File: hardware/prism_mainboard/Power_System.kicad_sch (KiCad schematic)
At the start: 0 parts

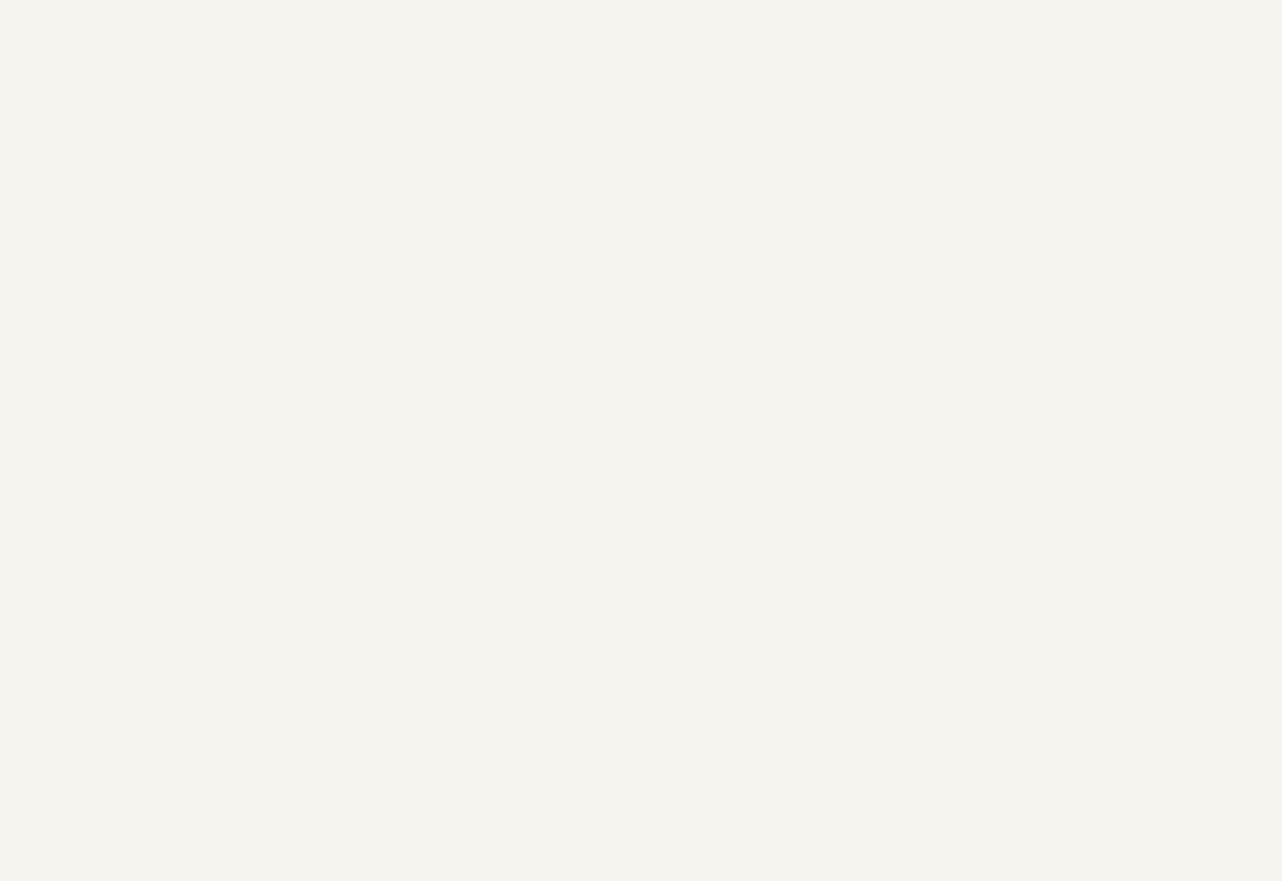
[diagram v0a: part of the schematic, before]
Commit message: KiCAD Update
Added Power System Schematics. Decided on a 4 in 1 Buck and LDO, LP87222TQ1, for 3.3V and 1.8V LDO, and 1.8V and 1.0V Buck converter.
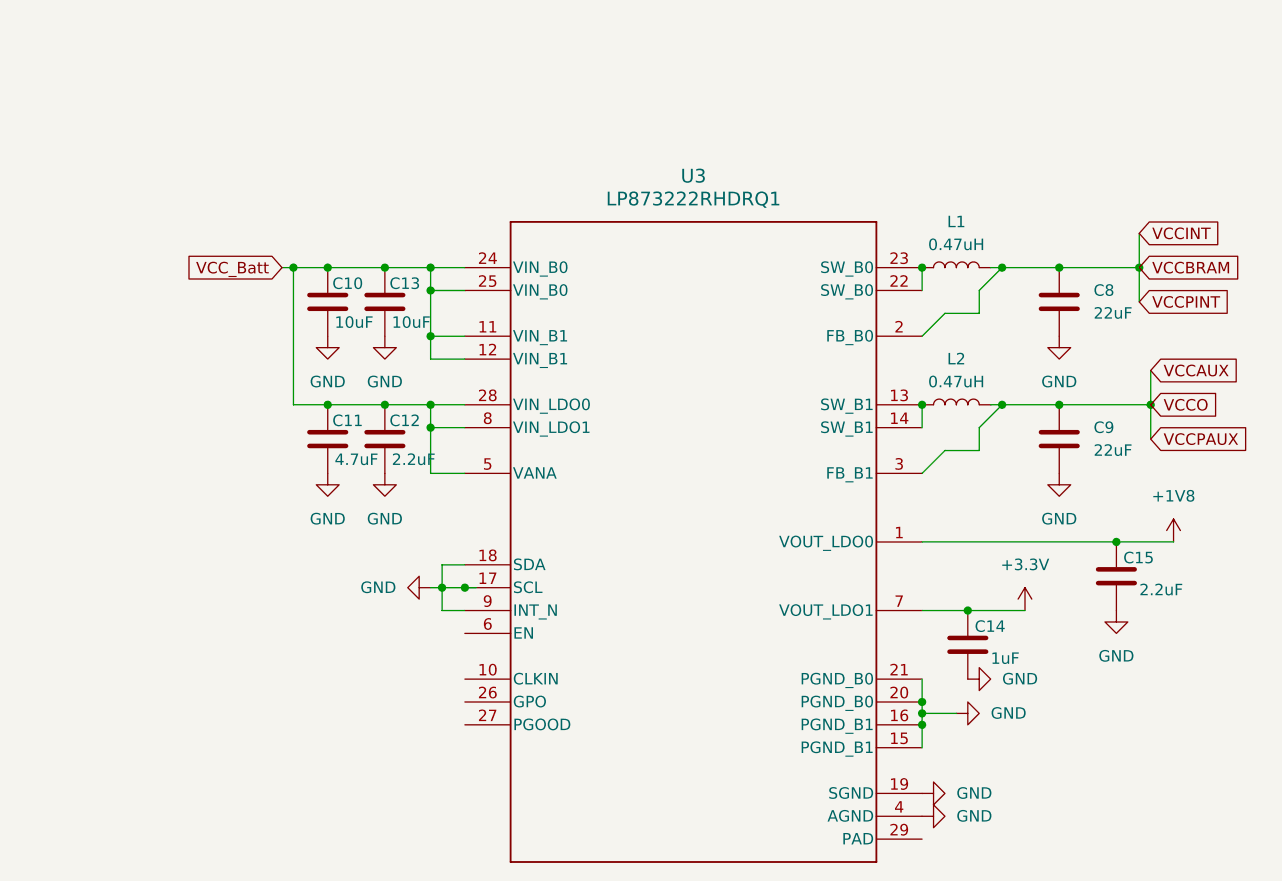
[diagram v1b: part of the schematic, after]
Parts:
- added C10, C13: 10uF, Capacitor_SMD:C_0805_2012Metric, symbol Device:C
- added C11: 4.7uF, Capacitor_SMD:C_0805_2012Metric, symbol Device:C
- added C12, C15: 2.2uF, Capacitor_SMD:C_0201_0603Metric, symbol Device:C
- added C14: 1uF, Capacitor_SMD:C_0201_0603Metric, symbol Device:C
- added C8, C9: 22uF, Capacitor_SMD:C_1206_3216Metric, symbol Device:C
- added L1, L2: 0.47uH, Inductor_SMD:L_0805_2012Metric, symbol Device:L
- added U3: LP873222RHDRQ1, RHD0028W, symbol 2026-05-18_00-35-41:LP873222RHDRQ1
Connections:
- net VCCAUX: now also C9.1, L2.2
- net VCCBRAM: now also C8.1, L1.2
- net VCC_Batt: now also C10.1, C11.1, C12.1, C13.1, U3.11 (VIN_B1), U3.12 (VIN_B1), U3.24 (VIN_B0), U3.25 (VIN_B0), U3.28 (VIN_LDO0), U3.5 (VANA), U3.8 (VIN_LDO1)
- new net: L2.1, U3.13 (SW_B1), U3.14 (SW_B1)
- new net: L1.1, U3.22 (SW_B0), U3.23 (SW_B0)
- new net +1V8: C15.1, U3.1 (VOUT_LDO0)
- new net +3.3V: C14.1, U3.7 (VOUT_LDO1)
- new net GND: C10.2, C11.2, C12.2, C13.2, C14.2, C15.2, C8.2, C9.2, U3.15 (PGND_B1), U3.16 (PGND_B1), U3.17 (SCL), U3.18 (SDA), U3.19 (SGND), U3.20 (PGND_B0), U3.21 (PGND_B0), U3.4 (AGND), U3.9 (INT_N)

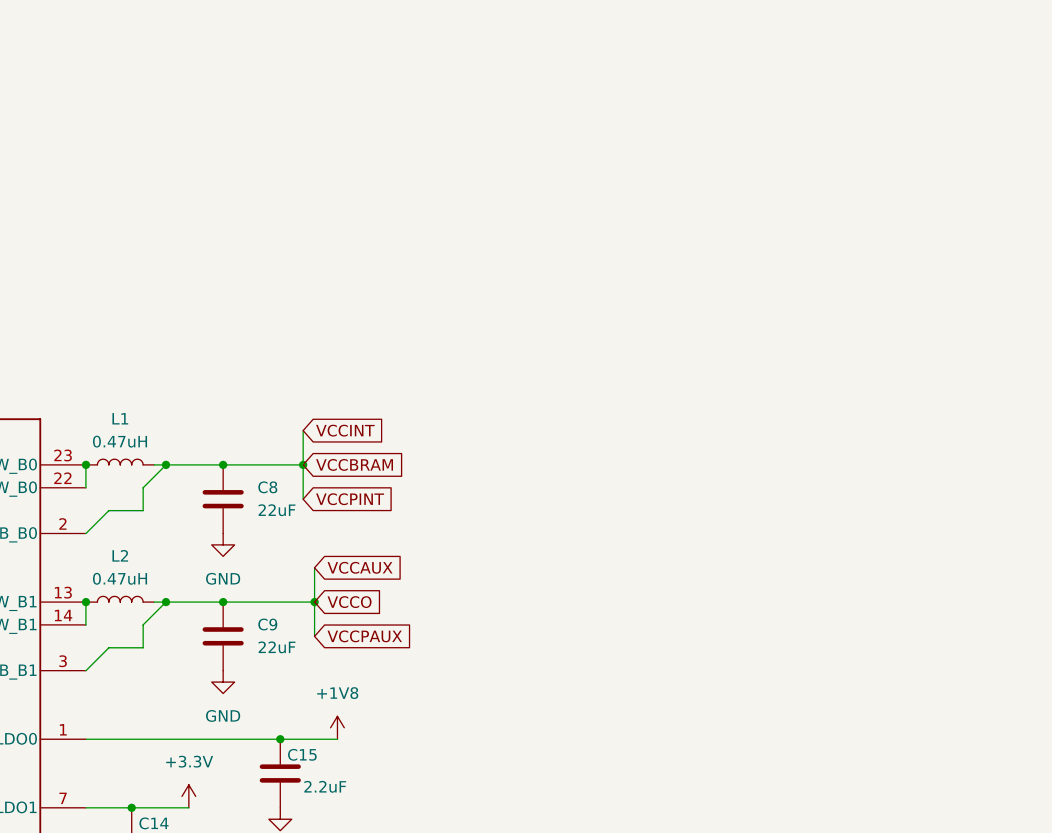
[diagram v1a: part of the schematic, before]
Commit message: Schematics
More schematics updates, moving to Desktop for editing. Continued with power usage, debating use of Dedicated DDR3/3L power IC instead of using LDO and Buck from mainboard power.
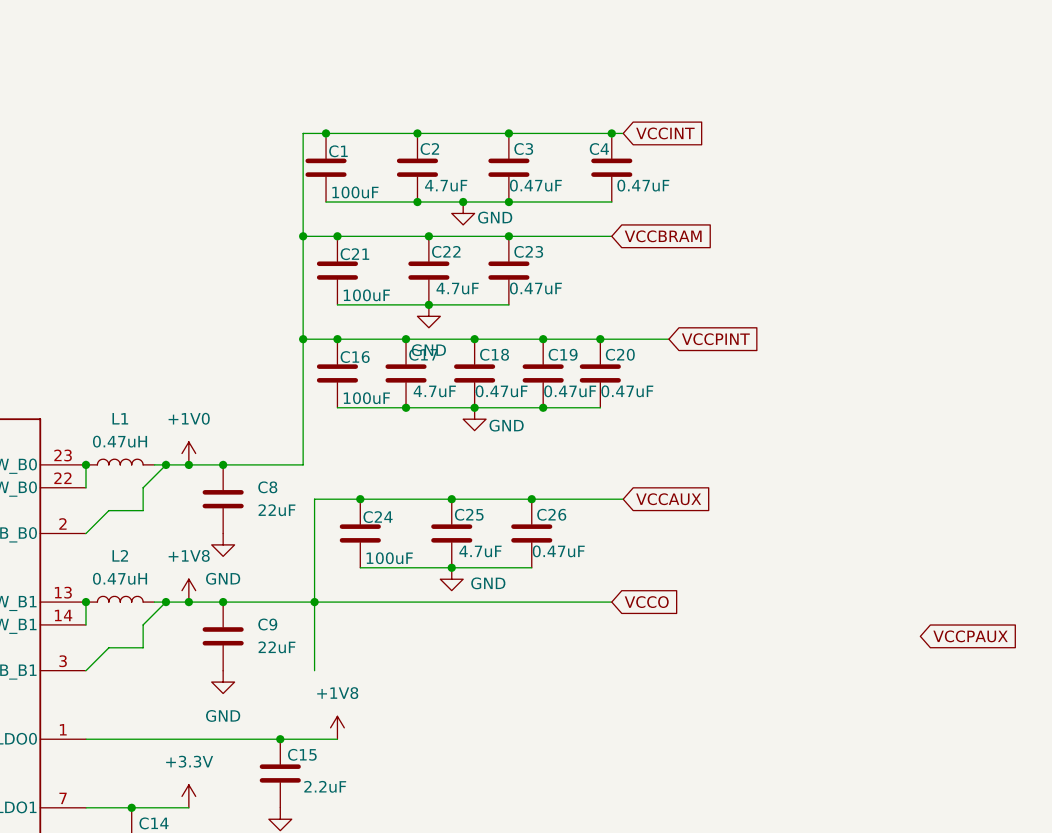
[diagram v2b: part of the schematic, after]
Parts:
- added C1, C16, C21, C24: 100uF, symbol Device:C
- added C17, C2, C22, C25: 4.7uF, symbol Device:C
- added C18, C19, C20, C23, C26, C3, C4: 0.47uF, symbol Device:C
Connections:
- net VCCAUX is gone; now on net +1V8: C9.1, L2.2
- net +1V8: now also C24.1, C25.1, C26.1
- net GND: now also C1.2, C16.2, C17.2, C18.2, C19.2, C2.2, C20.2, C21.2, C22.2, C23.2, C24.2, C25.2, C26.2, C3.2, C4.2
- net VCCBRAM renamed +1V0
- net +1V0: now also C1.1, C16.1, C17.1, C18.1, C19.1, C2.1, C20.1, C21.1, C22.1, C23.1, C3.1, C4.1

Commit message: Removed Protoflow
Removed protoflow because it has not advanced enough to help in any substantial way, going back to KiCAD
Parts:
- added C27, C28: 22uF, ProtoFlow.pretty:C0805, symbol Device:C
- added U4: 100uF, symbol Device:C
- added U5: 0.47uF, symbol Device:C
- added U6: 4.7uF, symbol Device:C
- added U7: GND, symbol power:GND
- C1, C10, C11, C12, C13, C14, C15, C16, C17, C18, C19, C2, C20, C21, C22, C23, C24, C25, C26, C3, C4, C8, C9, L1, L2, U3: Protoflow_Source (none) -> kicad
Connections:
- net VCCBRAM: now reaches U3.2 (FB_B0)
- net VCCBRAM: now also C1.1, C16.1, C17.1, C18.1, C19.1, C20.1, C21.1, C22.1, C23.1, C4.1, C8.1, L1.2
- net VCCAUX: now reaches U3.3 (FB_B1)
- net VCCAUX: now also C24.1, C25.1, C26.1, C9.1, L2.2
- removed net +1V0: C1.1, C16.1, C17.1, C18.1, C19.1, C2.1, C20.1, C21.1, C22.1, C23.1, C3.1, C4.1, C8.1, L1.2
- removed net +1V8: C15.1, C24.1, C25.1, C26.1, C9.1, L2.2, U3.1 (VOUT_LDO0)
- net +3.3V: no longer names the net of C14.1, U3.7 (VOUT_LDO1)
- removed net GND: C1.2, C10.2, C11.2, C12.2, C13.2, C14.2, C15.2, C16.2, C17.2, C18.2, C19.2, C2.2, C20.2, C21.2, C22.2, C23.2, C24.2, C25.2, C26.2, C3.2, C4.2, C8.2, C9.2, U3.15 (PGND_B1), U3.16 (PGND_B1), U3.17 (SCL), U3.18 (SDA), U3.19 (SGND), U3.20 (PGND_B0), U3.21 (PGND_B0), U3.4 (AGND), U3.9 (INT_N)
- new net: C16.2, C17.2, C18.2, C19.2, C20.2
- new net: C15.1, U3.1 (VOUT_LDO0)
- new net: C1.2, C2.2, C3.2, C4.2
- new net: C24.2, C25.2, C26.2
- new net: U4.2, U5.2, U6.2, U7.1
- new net: U3.15 (PGND_B1), U3.16 (PGND_B1), U3.20 (PGND_B0), U3.21 (PGND_B0)
- new net: U3.17 (SCL), U3.18 (SDA), U3.9 (INT_N)
- new net: C21.2, C22.2, C23.2
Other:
- company: (none) -> Protoflow
- title: (none) -> Untitled
